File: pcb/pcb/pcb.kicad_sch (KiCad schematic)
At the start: 5 parts, among them U1 XIAO-RP2040-DIP, U2 XIAO-RP2040-DIP, U3 L298N, U4 L298N, U5 MPU-6050

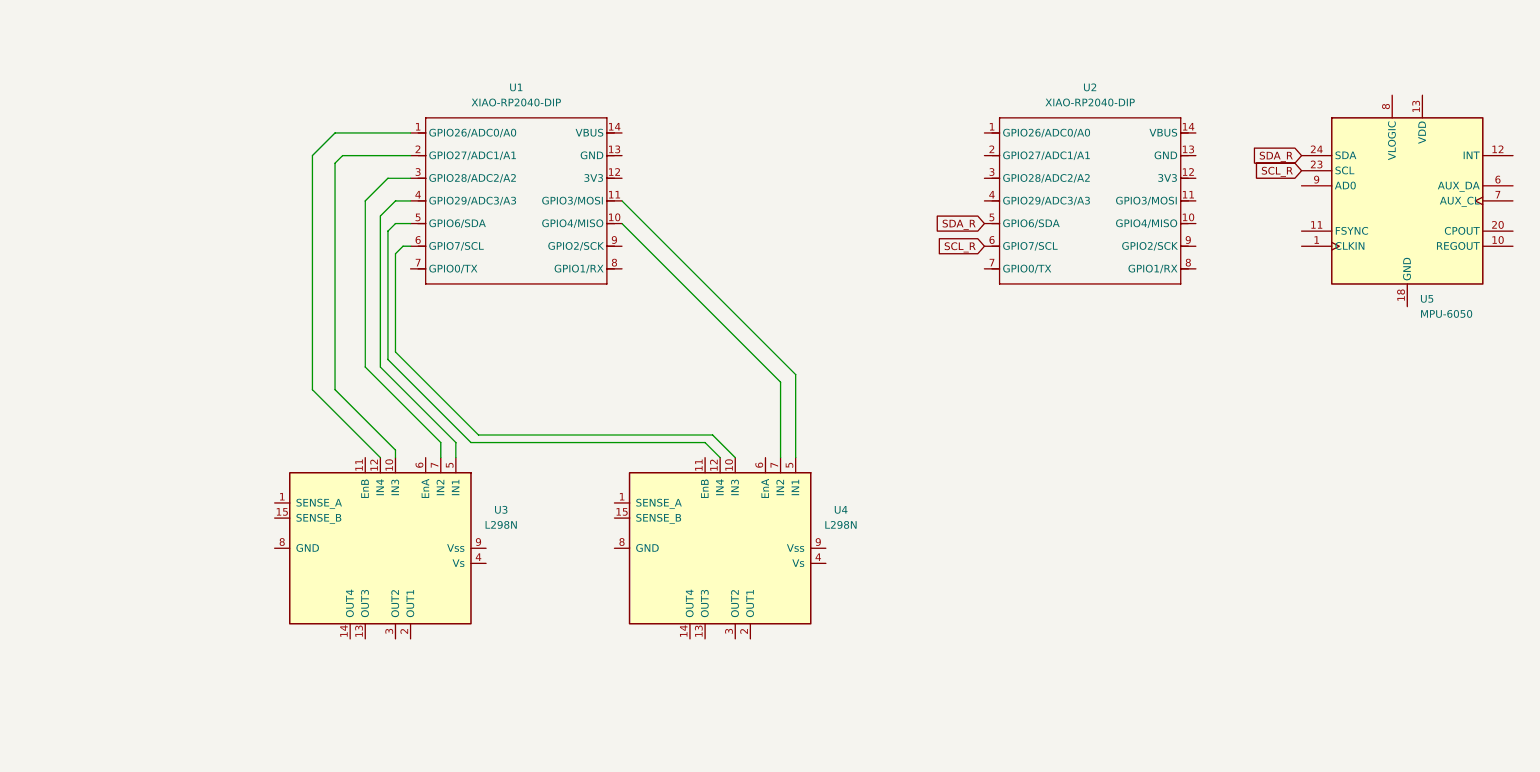
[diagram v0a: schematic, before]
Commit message: update readme w/ motors
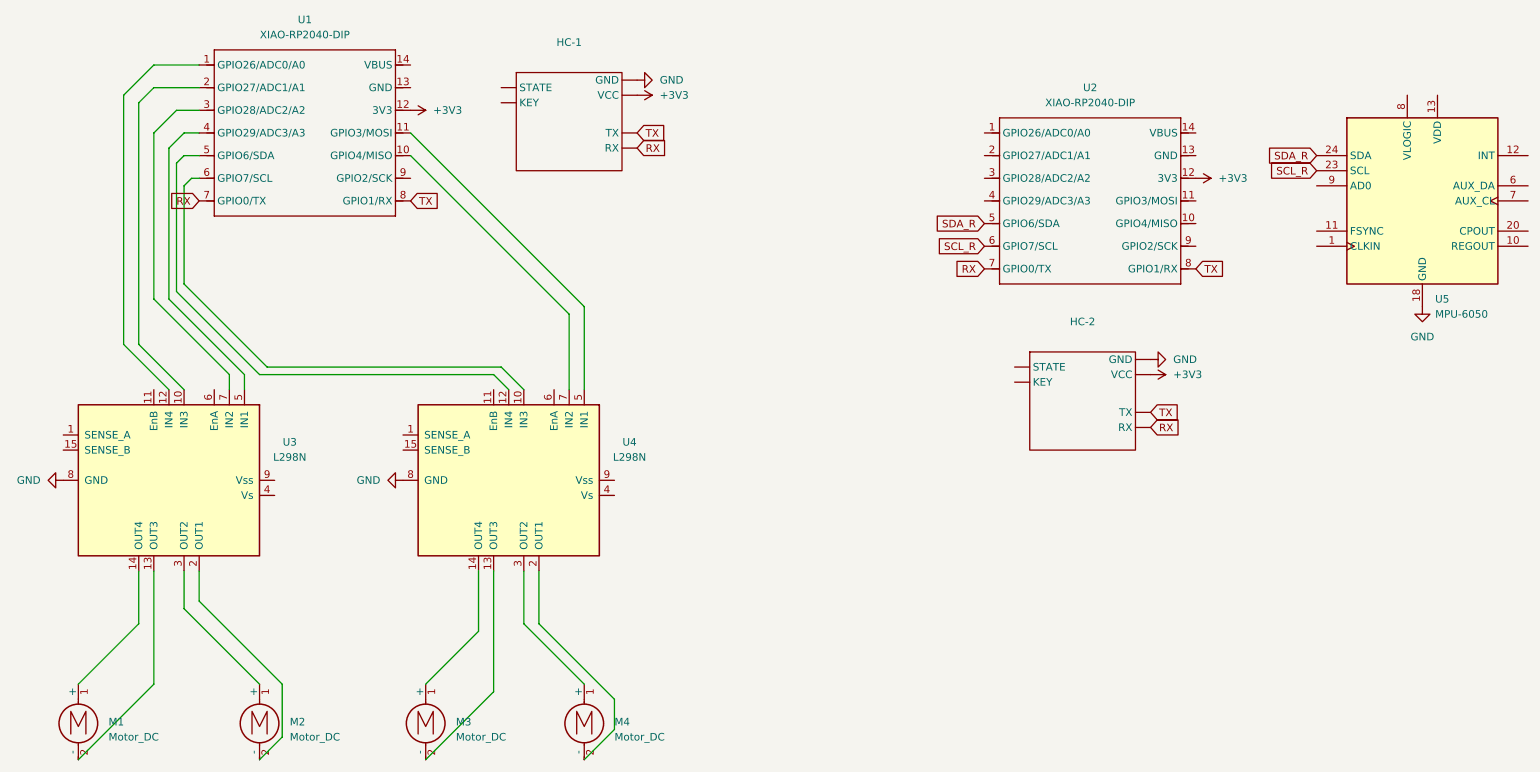
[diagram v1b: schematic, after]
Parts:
- added HC-1, HC-2: ~, symbol hc05:HC-05BLE
- added M1, M2, M3, M4: Motor_DC, symbol Motor:Motor_DC
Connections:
- net +3V3: now reaches U2.12 (3V3)
- net +3V3: now also U1.12 (3V3), HC-1. (RX), HC-2. (RX)
- net RX: now reaches U2.7 (GPIO0/TX)
- net RX: now also U1.7 (GPIO0/TX), HC-1. (RX), HC-2. (RX)
- net TX: now reaches U2.8 (GPIO1/RX)
- net TX: now also U1.8 (GPIO1/RX), HC-1. (RX), HC-2. (RX)
- net at U4.13 (OUT3): now also M3.2 (-)
- net at U4.14 (OUT4): now also M3.1 (+)
- net at U4.2 (OUT1): now also M4.2 (-)
- net at U4.3 (OUT2): now also M4.1 (+)
- net GND: now reaches U4.8 (GND)
- net GND: now also U3.8 (GND), U5.18 (GND), HC-1. (RX), HC-2. (RX)
- net at U3.13 (OUT3): now also M1.2 (-)
- net at U3.14 (OUT4): now also M1.1 (+)
- net at U3.2 (OUT1): now also M2.2 (-)
- net at U3.3 (OUT2): now also M2.1 (+)
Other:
- moved on the sheet: U1, U3, U4, U5
